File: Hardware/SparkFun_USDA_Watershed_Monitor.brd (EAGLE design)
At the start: 63.5 x 63.5 mm, 232 parts, among them J10 QWIIC_RIGHT_ANGLE, J3 QWIIC_RIGHT_ANGLE, J4 U.FL, J5 RJ45, J7 RJ45, J9 RJ45, Q1 20V/4.2A/52mΩ/1.4W, Q2 20V/0.2A/8MHz/1.2Ω/1Vth, Q3 20V/0.2A/8MHz/1.2Ω/1Vth, Q4 20V/0.2A/8MHz/1.2Ω/1Vth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

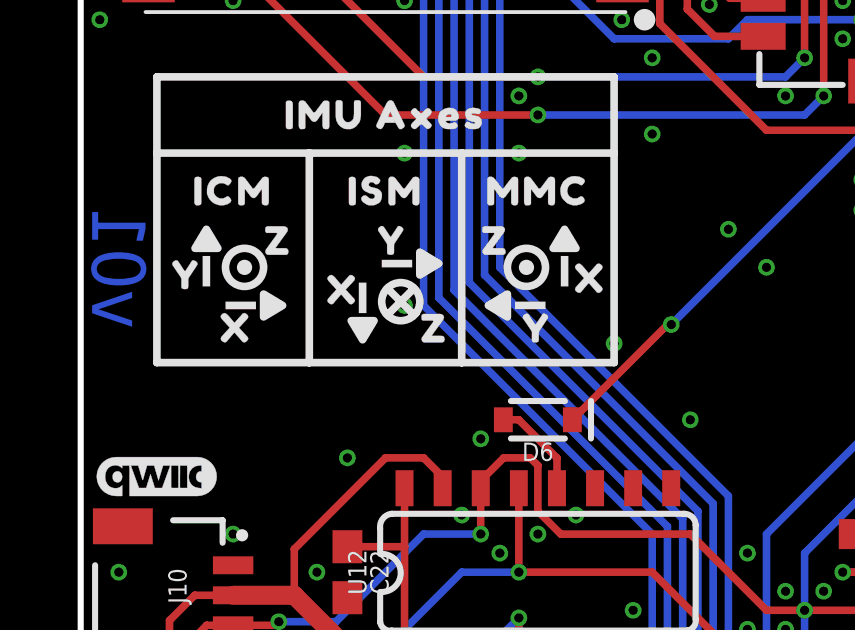
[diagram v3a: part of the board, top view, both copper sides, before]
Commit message: Add MMC I2C address to schematic
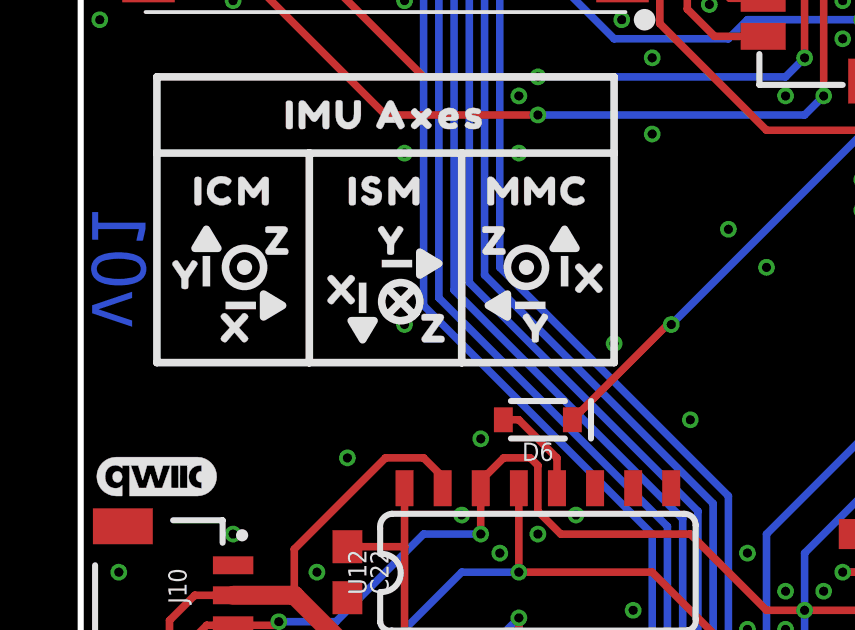
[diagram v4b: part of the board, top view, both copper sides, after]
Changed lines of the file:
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@@
 <via x="7.62" y="17.78" extent="1-16" drill="0.3048"/>
 <via x="10.795" y="35.56" extent="1-16" drill="0.3048"/>
-<via x="10.795" y="30.48" extent="1-16" drill="0.3048"/>
+<via x="10.795" y="29.845" extent="1-16" drill="0.3048"/>
 <via x="13.335" y="26.035" extent="1-16" drill="0.3048"/>
 <via x="17.78" y="29.21" extent="1-16" drill="0.3048"/>

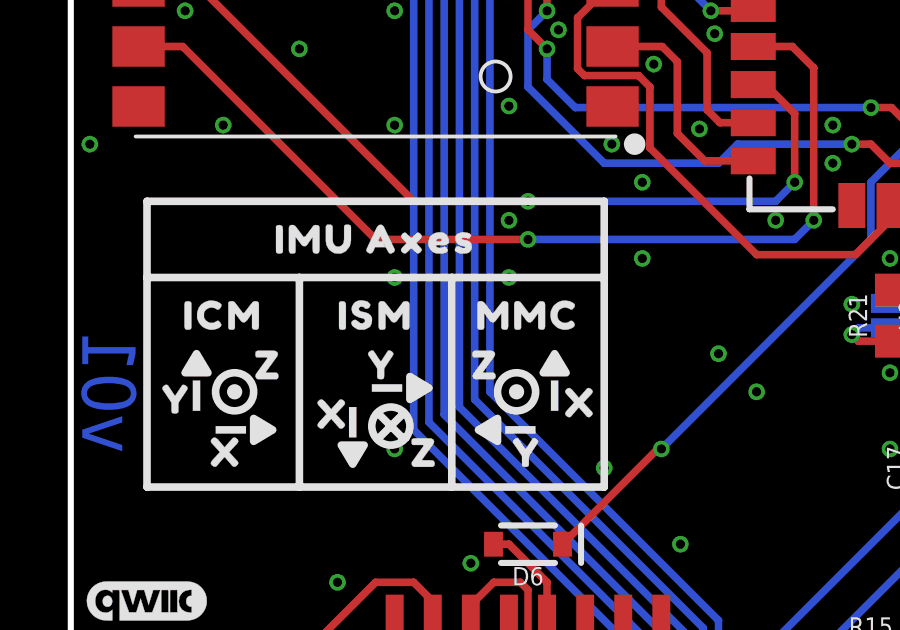
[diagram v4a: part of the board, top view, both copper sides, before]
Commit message: Fix ISM and MMC axis silk labels
They were flipped, just swapped the names
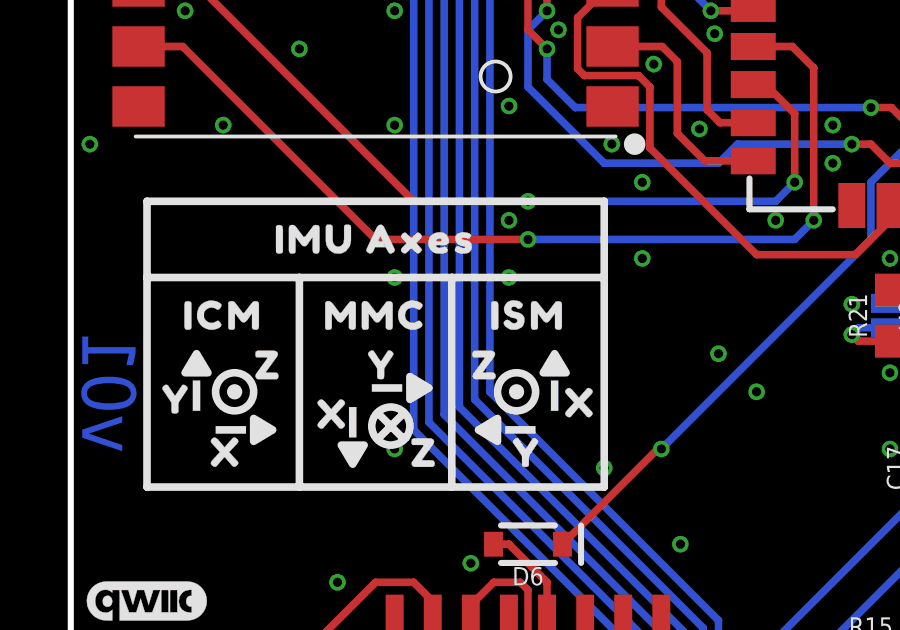
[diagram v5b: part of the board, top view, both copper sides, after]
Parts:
- moved U$111 5.08 mm to (15.2, 34.3)
- moved U$112 5.08 mm to (10.2, 34.3)
- moved U$98 5.08 mm to (15.2, 34.3)
- moved U$99 5.08 mm to (10.2, 34.3)
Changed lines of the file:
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@@
 <layer number="46" name="Milling" color="3" fill="1" visible="yes" active="yes"/>
 <layer number="47" name="Measures" color="7" fill="1" visible="yes" active="yes"/>
-<layer number="48" name="Document" color="7" fill="1" visible="no" active="yes"/>
+<layer number="48" name="Document" color="7" fill="1" visible="yes" active="yes"/>
 <layer number="49" name="Reference" color="7" fill="1" visible="no" active="yes"/>
 <layer number="50" name="dxf" color="7" fill="1" visible="no" active="no"/>
@@
 <element name="U$96" library="output" package="Z0" value="" x="13.843" y="32.639" smashed="yes"/>
 <element name="U$97" library="output" package="ICM0" value="" x="5.08" y="34.29" smashed="yes"/>
-<element name="U$98" library="output" package="ISM0" value="" x="10.16" y="34.29" smashed="yes"/>
-<element name="U$99" library="output" package="MMC0" value="" x="15.24" y="34.29" smashed="yes"/>
+<element name="U$98" library="output" package="ISM0" value="" x="15.24" y="34.29" smashed="yes"/>
+<element name="U$99" library="output" package="MMC0" value="" x="10.16" y="34.29" smashed="yes"/>
 <element name="U$101" library="output" package="IMU_AXES0" value="" x="10.16" y="36.83" smashed="yes"/>
 <element name="U$100" library="output" package="X0" value="" x="5.08" y="29.718" smashed="yes" rot="MR0"/>
@@
 <element name="U$109" library="output" package="Z0" value="" x="13.716" y="32.639" smashed="yes" rot="MR0"/>
 <element name="U$110" library="output" package="ICM0" value="" x="5.08" y="34.29" smashed="yes" rot="MR0"/>
-<element name="U$111" library="output" package="ISM0" value="" x="10.16" y="34.29" smashed="yes" rot="MR0"/>
-<element name="U$112" library="output" package="MMC0" value="" x="15.24" y="34.29" smashed="yes" rot="MR0"/>
+<element name="U$111" library="output" package="ISM0" value="" x="15.24" y="34.29" smashed="yes" rot="MR0"/>
+<element name="U$112" library="output" package="MMC0" value="" x="10.16" y="34.29" smashed="yes" rot="MR0"/>
 <element name="U$113" library="output" package="IMU_AXES0" value="" x="10.16" y="36.83" smashed="yes" rot="MR0"/>
 <element name="LOGO5" library="SparkFun-Aesthetics" package="SFE_LOGO_NAME_FLAME_.1" value="SFE_LOGO_NAME_FLAME.1_INCH" x="46.99" y="59.055" smashed="yes" rot="MR0"/>

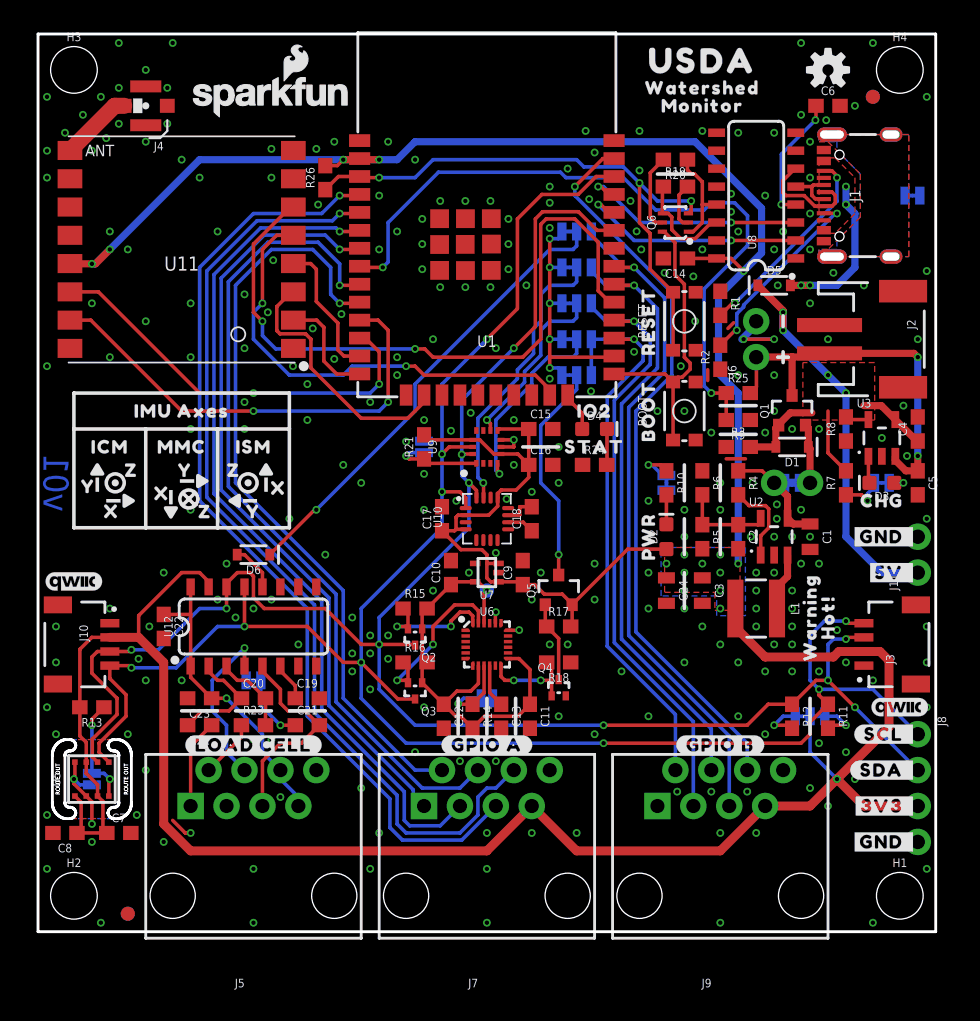
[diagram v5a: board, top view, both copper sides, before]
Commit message: Add VOUT net for GPIO A, left Qwiic, and load cell
Controlled by a P-channel MOSFET, had to steal GPIO16
Also changed "5V" label to "5V IN"
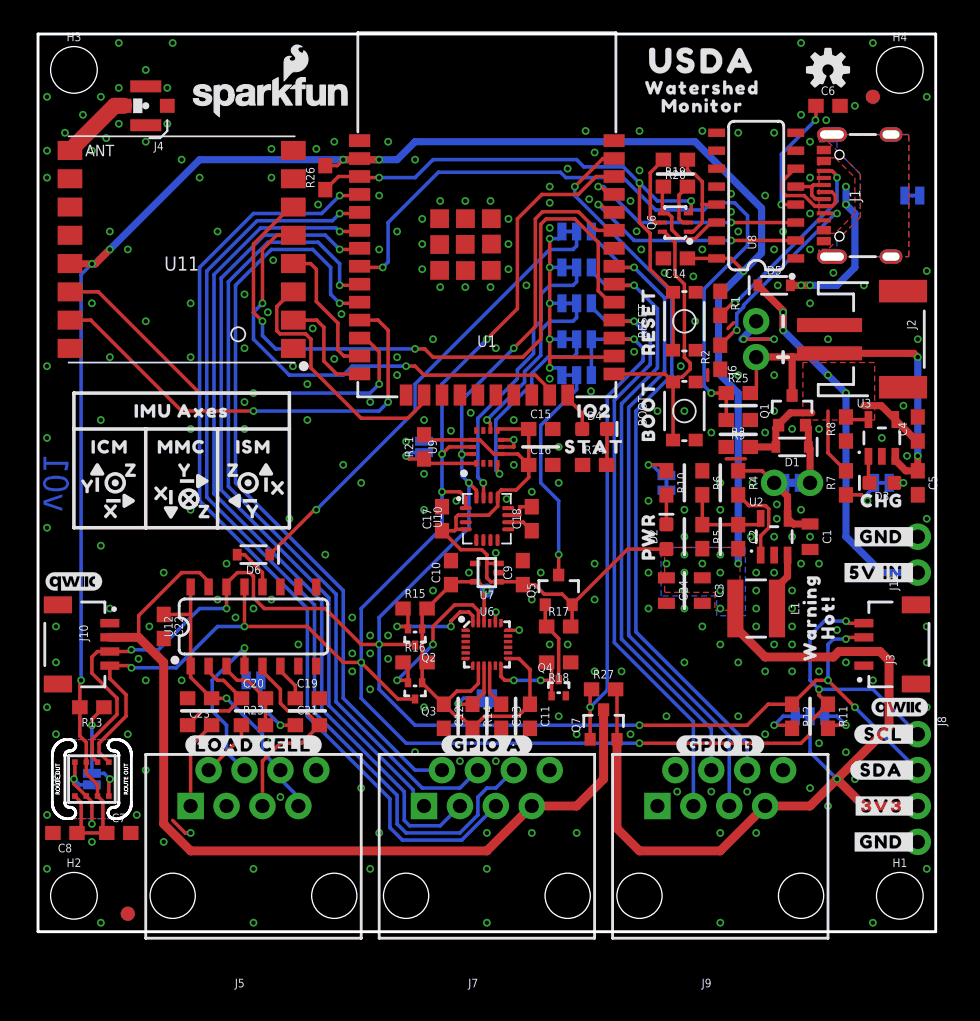
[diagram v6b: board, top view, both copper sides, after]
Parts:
- removed U$82: (no value), output:#5V_#0
- removed U$83: (no value), output:#_5V#6
- added Q7: 20V/4.2A/52mΩ/1.4W, SparkFun-DiscreteSemi:SOT23-3
- added R27: 100k, SparkFun-Resistors:0603
- added U$117: (no value), output:#5V_IN_#0
- added U$118: (no value), output:#_5V_IN#0
- U$57: device output:IO160 -> output:NC0
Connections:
- new net VOUT: J10.2, J7.7, Q7.3, U12.15
- net 3.3V: now also Q7.2, R27.2; no longer J10.2, J7.7, U12.15
- net ESP_IO16: now also Q7.1, R27.1; no longer J9.2
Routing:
- net VOUT: track 0.00 -> 63.3 mm
- net 3.3V: track 271.9 -> 247.8 mm, vias 16 -> 17
- net ESP_IO16: track 40.8 -> 38.4 mm, vias 1 -> 2
- net GND: vias 271 -> 277

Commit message: Update DNP component values and PROD_ID's
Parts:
- C15, C16: value 0.1uF -> DNP
- C17: value 1.0uF -> DNP
- C18: value 10uF -> DNP
- R21: value 100k -> DNP
- U10: value MMC5983MA_QFN16 -> DNP
- U9: value ISM330DHCX -> DNP
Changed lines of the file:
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@@
 <attribute name="VALUE" x="45.085" y="48.387" size="0.6096" layer="27" font="vector" ratio="20" rot="R180" align="top-center"/>
 </element>
-<element name="U9" library="SparkFun-Sensors" package="LGA-14L" value="ISM330DHCX" x="31.75" y="34.29" smashed="yes" rot="R90">
+<element name="U9" library="SparkFun-Sensors" package="LGA-14L" value="DNP" x="31.75" y="34.29" smashed="yes" rot="R90">
 <attribute name="NAME" x="27.901" y="34.29" size="0.6096" layer="25" font="vector" ratio="20" rot="R90" align="center"/>
-<attribute name="PROD_ID" value="IC-16693" x="31.75" y="34.29" size="1.778" layer="27" font="vector" ratio="15" rot="R90" display="off"/>
+<attribute name="PROD_ID" value="" x="31.75" y="34.29" size="1.778" layer="27" font="vector" ratio="15" rot="R90" display="off"/>
 <attribute name="VALUE" x="33.496" y="34.29" size="0.6096" layer="27" font="vector" ratio="20" rot="R90" align="center"/>
 </element>
-<element name="U10" library="SparkFun-Sensors" package="LGA-16-3X3MM-4X4PINS" value="MMC5983MA_QFN16" x="31.75" y="29.21" smashed="yes" rot="R90">
+<element name="U10" library="SparkFun-Sensors" package="LGA-16-3X3MM-4X4PINS" value="DNP" x="31.75" y="29.21" smashed="yes" rot="R90">
 <attribute name="NAME" x="28.575" y="28.575" size="0.6096" layer="25" font="vector" ratio="20" rot="R90"/>
-<attribute name="PROD_ID" value="IC-16314" x="31.75" y="29.21" size="1.778" layer="27" font="vector" ratio="15" rot="R90" display="off"/>
+<attribute name="PROD_ID" value="" x="31.75" y="29.21" size="1.778" layer="27" font="vector" ratio="15" rot="R90" display="off"/>
 <attribute name="VALUE" x="33.02" y="28.575" size="0.6096" layer="27" font="vector" ratio="20" rot="R90"/>
 </element>
-<element name="C15" library="SparkFun-Capacitors" package="0603" value="0.1uF" x="35.56" y="35.56" smashed="yes">
+<element name="C15" library="SparkFun-Capacitors" package="0603" value="DNP" x="35.56" y="35.56" smashed="yes">
 <attribute name="NAME" x="35.56" y="36.322" size="0.6096" layer="25" font="vector" ratio="20" align="bottom-center"/>
-<attribute name="PROD_ID" value="CAP-00810" x="35.56" y="35.56" size="1.778" layer="27" font="vector" ratio="15" display="off"/>
+<attribute name="PROD_ID" value="" x="35.56" y="35.56" size="1.778" layer="27" font="vector" ratio="15" display="off"/>
 <attribute name="VALUE" x="35.56" y="34.798" size="0.6096" layer="27" font="vector" ratio="20" align="top-center"/>
 </element>
-<element name="C16" library="SparkFun-Capacitors" package="0603" value="0.1uF" x="35.56" y="33.02" smashed="yes">
+<element name="C16" library="SparkFun-Capacitors" package="0603" value="DNP" x="35.56" y="33.02" smashed="yes">
 <attribute name="NAME" x="35.56" y="33.782" size="0.6096" layer="25" font="vector" ratio="20" align="bottom-center"/>
-<attribute name="PROD_ID" value="CAP-00810" x="35.56" y="33.02" size="1.778" layer="27" font="vector" ratio="15" display="off"/>
+<attribute name="PROD_ID" value="" x="35.56" y="33.02" size="1.778" layer="27" font="vector" ratio="15" display="off"/>
 <attribute name="VALUE" x="35.56" y="32.258" size="0.6096" layer="27" font="vector" ratio="20" align="top-center"/>
 </element>
-<element name="C17" library="SparkFun-Capacitors" package="0603" value="1.0uF" x="28.575" y="29.21" smashed="yes" rot="R90">
+<element name="C17" library="SparkFun-Capacitors" package="0603" value="DNP" x="28.575" y="29.21" smashed="yes" rot="R90">
 <attribute name="NAME" x="27.813" y="29.21" size="0.6096" layer="25" font="vector" ratio="20" rot="R90" align="bottom-center"/>
-<attribute name="PROD_ID" value="CAP-00868" x="28.575" y="29.21" size="1.778" layer="27" font="vector" ratio="15" rot="R90" display="off"/>
+<attribute name="PROD_ID" value="" x="28.575" y="29.21" size="1.778" layer="27" font="vector" ratio="15" rot="R90" display="off"/>
 <attribute name="VALUE" x="29.337" y="29.21" size="0.6096" layer="27" font="vector" ratio="20" rot="R90" align="top-center"/>
 </element>
-<element name="C18" library="SparkFun-Capacitors" package="0603" value="10uF" x="34.925" y="29.21" smashed="yes" rot="R90">
+<element name="C18" library="SparkFun-Capacitors" package="0603" value="DNP" x="34.925" y="29.21" smashed="yes" rot="R90">
 <attribute name="NAME" x="34.163" y="29.21" size="0.6096" layer="25" font="vector" ratio="20" rot="R90" align="bottom-center"/>
-<attribute name="PROD_ID" value="CAP-11015" x="34.925" y="29.21" size="1.778" layer="27" font="vector" ratio="15" rot="R90" display="off"/>
+<attribute name="PROD_ID" value="" x="34.925" y="29.21" size="1.778" layer="27" font="vector" ratio="15" rot="R90" display="off"/>
 <attribute name="VALUE" x="35.687" y="29.21" size="0.6096" layer="27" font="vector" ratio="20" rot="R90" align="top-center"/>
 </element>
-<element name="R21" library="SparkFun-Resistors" package="0603" value="100k" x="27.305" y="34.29" smashed="yes" rot="R90">
+<element name="R21" library="SparkFun-Resistors" package="0603" value="DNP" x="27.305" y="34.29" smashed="yes" rot="R90">
 <attribute name="NAME" x="26.543" y="34.29" size="0.6096" layer="25" font="vector" ratio="20" rot="R90" align="bottom-center"/>
-<attribute name="PROD_ID" value="RES-07828" x="23.495" y="34.29" size="1.778" layer="27" font="vector" ratio="15" rot="R90" display="off"/>
+<attribute name="PROD_ID" value="" x="23.495" y="34.29" size="1.778" layer="27" font="vector" ratio="15" rot="R90" display="off"/>
 <attribute name="VALUE" x="28.067" y="34.29" size="0.6096" layer="27" font="vector" ratio="20" rot="R90" align="top-center"/>
 </element>
